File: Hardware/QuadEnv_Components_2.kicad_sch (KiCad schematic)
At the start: 54 parts, among them J1 Conn_01x04_Male, J2 Conn_01x05_Male, J3 Conn_01x04_Male, J4 Conn_01x04_Male, J5 SWD_Header, J6 Eurorack_10_pin_power, J7 USB_B_Micro, U1 STM32G431C6T6, U2 LD1117-3.3-4Tab, U3 CD40109B, U4 TL074

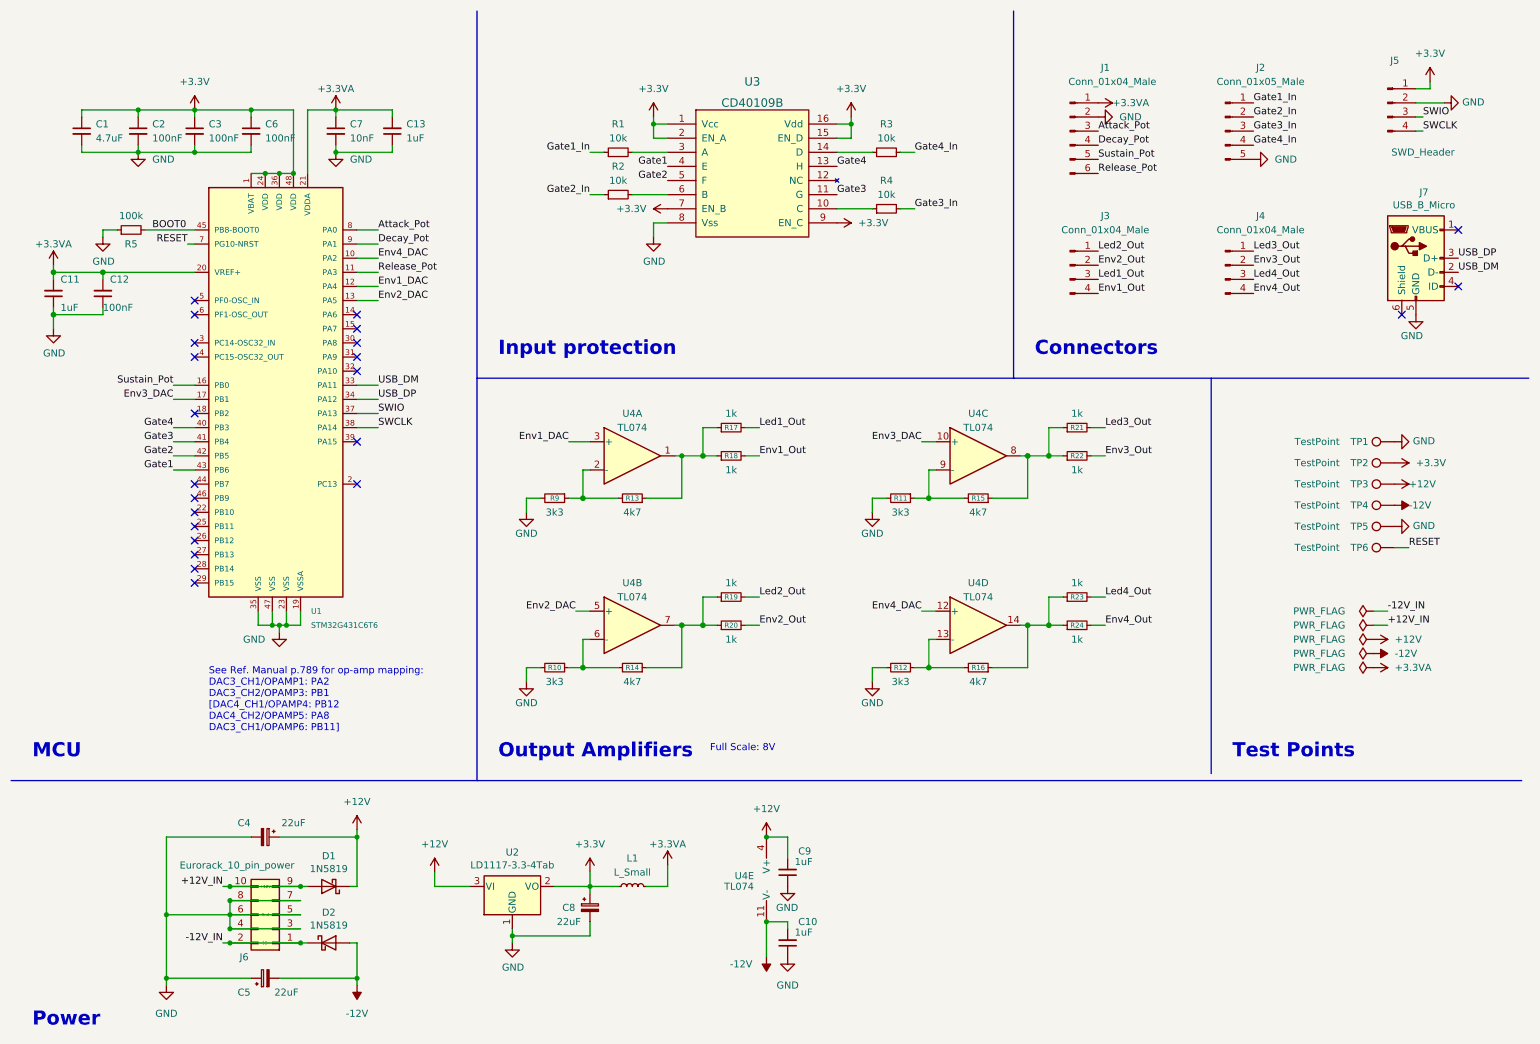
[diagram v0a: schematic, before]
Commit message: Updated components and controls to include mode button/led
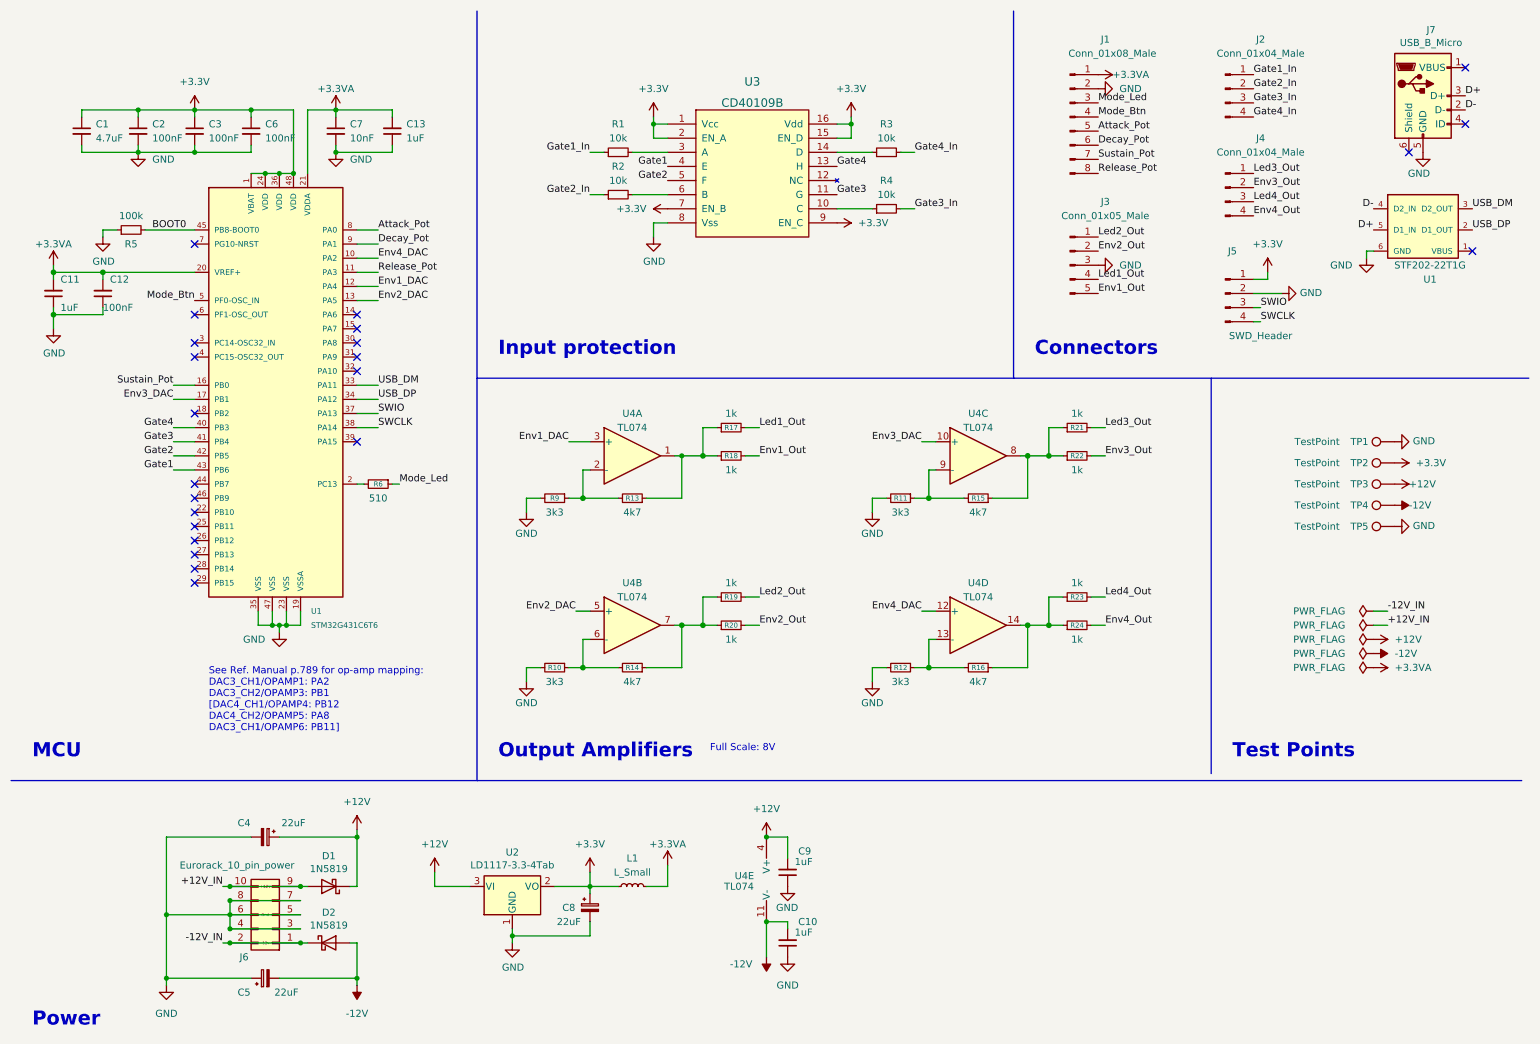
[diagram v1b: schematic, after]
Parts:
- removed TP6: TestPoint, Custom_Footprints:1mm_Test_Point, symbol Connector:TestPoint
- added R6: 510, Resistor_SMD:R_0603_1608Metric, symbol Device:R_Small
- added U1: STF202-22T1G, Custom_Footprints:STF202-22T1G, symbol STF202-22T1G:STF202-22T1G
- J1: value Conn_01x04_Male -> Conn_01x08_Male; footprint Connector_PinSocket_2.54mm:PinSocket_1x06_P2.54mm_Vertical -> Connector_PinHeader_2.54mm:PinHeader_1x08_P2.54mm_Vertical; symbol Connector:Conn_01x06_Male -> Connector:Conn_01x08_Pin
- J2: value Conn_01x05_Male -> Conn_01x04_Male; footprint Connector_PinSocket_2.54mm:PinSocket_1x05_P2.54mm_Vertical -> Connector_PinHeader_2.54mm:PinHeader_1x04_P2.54mm_Vertical; symbol Connector:Conn_01x05_Male -> Connector:Conn_01x04_Pin
- J3: value Conn_01x04_Male -> Conn_01x05_Male; footprint Connector_PinSocket_2.54mm:PinSocket_1x04_P2.54mm_Vertical -> Connector_PinHeader_2.54mm:PinHeader_1x05_P2.54mm_Vertical; symbol Connector:Conn_01x04_Male -> Connector:Conn_01x05_Pin
- J4: footprint Connector_PinSocket_2.54mm:PinSocket_1x04_P2.54mm_Vertical -> Connector_PinHeader_2.54mm:PinHeader_1x04_P2.54mm_Vertical; symbol Connector:Conn_01x04_Male -> Connector:Conn_01x04_Pin
- J5: symbol Connector:Conn_01x04_Male -> Connector:Conn_01x04_Pin
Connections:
- net Attack_Pot: now also J1.5 (Pin_5); no longer J1.3 (Pin_3)
- net Decay_Pot: now also J1.6 (Pin_6); no longer J1.4 (Pin_4)
- net Env1_Out: now also J3.5 (Pin_5); no longer J3.4 (Pin_4)
- net GND: now also J3.3 (Pin_3), U1.6 (GND); no longer J2.5 (Pin_5)
- net Led1_Out: now also J3.4 (Pin_4); no longer J3.3 (Pin_3)
- net Release_Pot: now also J1.8 (Pin_8); no longer J1.6 (Pin_6)
- net Sustain_Pot: now also J1.7 (Pin_7); no longer J1.5 (Pin_5)
- net USB_DM: now also U1.3 (D2_OUT); no longer J7.2 (D-)
- net USB_DP: now also U1.2 (D1_OUT); no longer J7.3 (D+)
- net at U1.2 (PC13): now also R6.2
- net Mode_Btn: now reaches U1.5 (PF0-OSC_IN)
- net Mode_Btn: now also J1.4 (Pin_4)
- net RESET: no longer names the net of U1.7 (PG10-NRST)
- new net D+: J7.3 (D+), U1.5 (D1_IN)
- new net D-: J7.2 (D-), U1.4 (D2_IN)
- new net Mode_Led: J1.3 (Pin_3), R6.1
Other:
- moved on the sheet: J4, J5, J7
